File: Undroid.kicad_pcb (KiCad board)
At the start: 4 copper layers, 61.7 x 133.2 mm, 40 parts

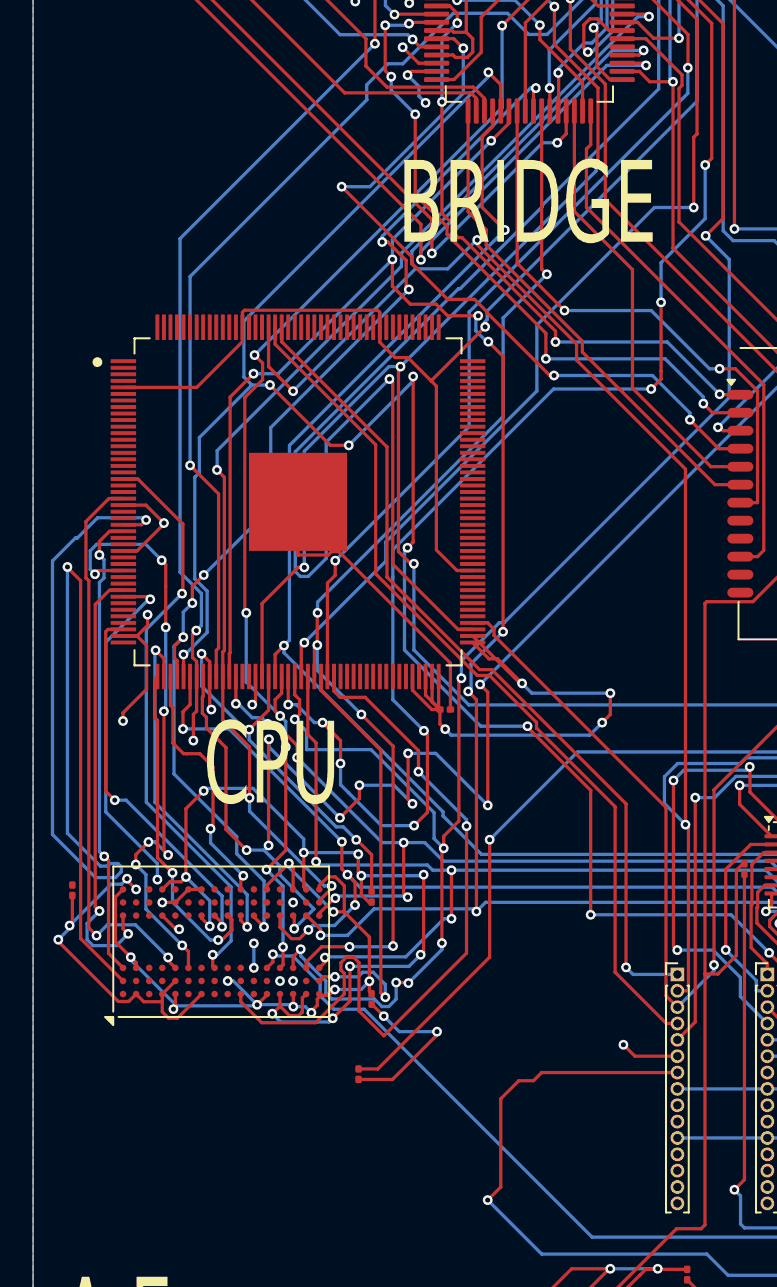
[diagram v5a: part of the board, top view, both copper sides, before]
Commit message: Improving routes.
Signed-off-by: Amlal EL Mahrouss <amlalelmahrouss@icloud.com>
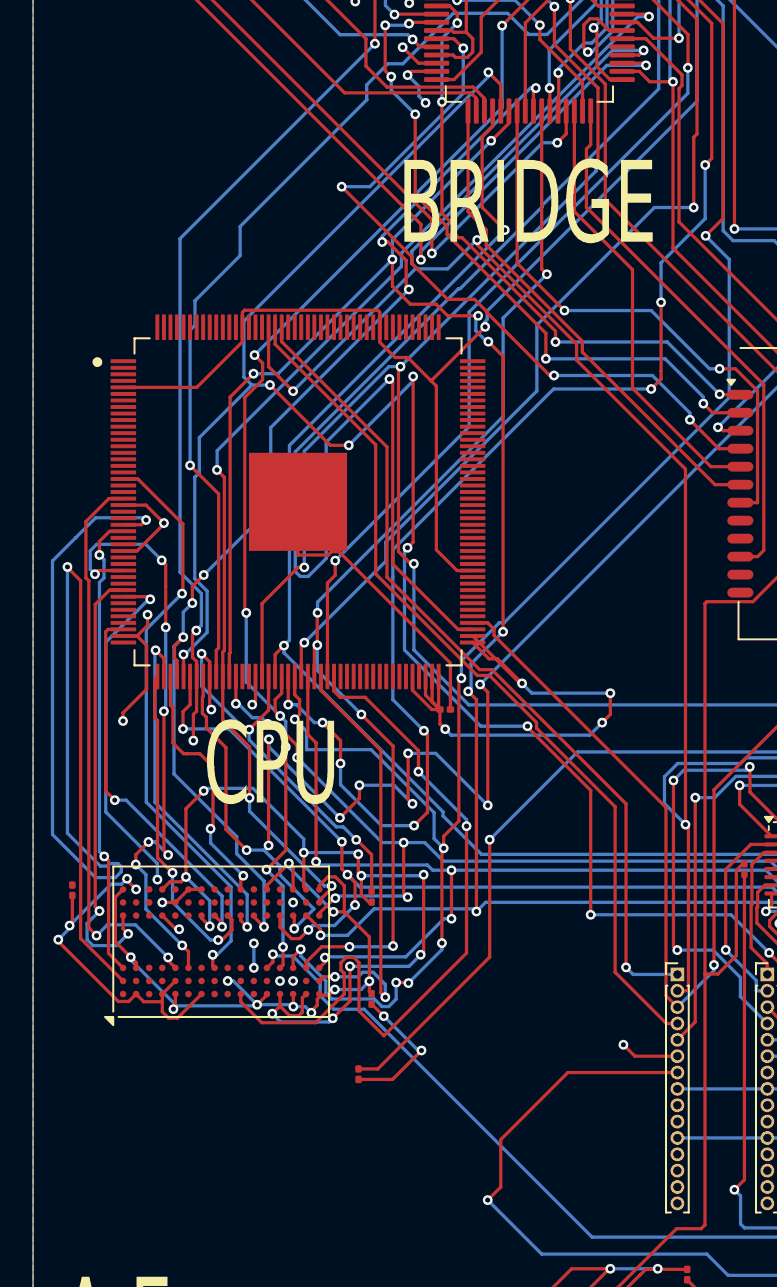
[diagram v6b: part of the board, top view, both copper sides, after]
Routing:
- net GND: track 96.6 -> 94.6 mm
- net GSM_RST_N: track 94.4 -> 92.9 mm
- net GSM_PWR_N: track 57.9 -> 56.6 mm
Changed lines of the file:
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@@
 	)
 	(segment
-		(start 160.3 144.7)
-		(end 157.935001 144.7)
+		(start 146.98 133.12)
+		(end 144.9 133.12)
 		(width 0.2)
 		(layer "F.Cu")
@@
 	)
 	(segment
-		(start 152.88 107.4)
-		(end 153.4 107.4)
+		(start 160.3 144.7)
+		(end 157.935001 144.7)
 		(width 0.2)
 		(layer "F.Cu")
@@
 	)
 	(segment
-		(start 149.7 130.2)
-		(end 149.7 130.4)
+		(start 152.88 107.4)
+		(end 153.4 107.4)
 		(width 0.2)
 		(layer "F.Cu")
@@
 	)
 	(segment
-		(start 149.7 130.4)
-		(end 146.98 133.12)
-		(width 0.2)
-		(layer "F.Cu")
-		(net 4)
-	)
-	(segment
 		(start 149.8 108.48)
 		(end 149.8 110.42)
@@
 	)
 	(segment
-		(start 162.7 66.2)
-		(end 162.475 65.975)
+		(start 148.75 131.35)
+		(end 146.98 133.12)
 		(width 0.2)
 		(layer "F.Cu")
@@
 	)
 	(segment
-		(start 146.98 133.12)
-		(end 144.9 133.12)
+		(start 162.7 66.2)
+		(end 162.475 65.975)
 		(width 0.2)
 		(layer "F.Cu")
@@
 	)
 	(via
-		(at 149.7 130.2)
+		(at 148.75 131.35)
 		(size 0.6)
 		(drill 0.3)
@@
 	)
 	(segment
+		(start 148.75 131.35)
+		(end 148.545818 131.35)
+		(width 0.2)
+		(layer "B.Cu")
+		(net 4)
+	)
+	(segment
 		(start 154.9 108.9)
 		(end 155.5 109.5)
@@
 	)
 	(segment
-		(start 147.395818 130.2)
-		(end 149.7 130.2)
-		(width 0.2)
-		(layer "B.Cu")
-		(net 4)
-	)
-	(segment
 		(start 159.0306 112.0694)
 		(end 150.5694 112.0694)
@@
 	)
 	(segment
-		(start 146.447909 129.252091)
-		(end 147.395818 130.2)
+		(start 148.545818 131.35)
+		(end 146.447909 129.252091)
 		(width 0.2)
 		(layer "B.Cu")
@@
 	)
 	(segment
+		(start 134.90015 87.00015)
+		(end 134.6003 87.3)
+		(width 0.2)
+		(layer "B.Cu")
+		(net 54)
+	)
+	(segment
 		(start 158.6439 65.5486)
 		(end 158.6439 67.0044)
@@
 	)
 	(segment
+		(start 137.66005 80.96005)
+		(end 137.66005 82.74025)
+		(width 0.2)
+		(layer "B.Cu")
+		(net 54)
+	)
+	(segment
 		(start 155.307 69.2172)
 		(end 154.0128 67.923)
@@
 	)
 	(segment
+		(start 137.66005 82.74025)
+		(end 134.90015 85.50015)
+		(width 0.2)
+		(layer "B.Cu")
+		(net 54)
+	)
+	(segment
 		(start 145.4 72.3)
 		(end 145.4 73.2)
@@
 	)
 	(segment
-		(start 134.6003 84.0198)
-		(end 134.6003 95.571)
+		(start 145.41005 73.21005)
+		(end 137.66005 80.96005)
 		(width 0.2)
 		(layer "B.Cu")
@@
 	)
 	(segment
-		(start 145.41005 73.21005)
-		(end 134.6003 84.0198)
+		(start 134.90015 85.50015)
+		(end 134.90015 87.00015)
+		(width 0.2)
+		(layer "B.Cu")
+		(net 54)
+	)
+	(segment
+		(start 134.6003 87.3)
+		(end 134.6003 95.571)
 		(width 0.2)
 		(layer "B.Cu")
@@
 	)
 	(segment
-		(start 127.7143 100.0005)
-		(end 127.7143 100.0006)
+		(start 129.5408 120.0746)
+		(end 129.1113 120.0746)
 		(width 0.2)
 		(layer "B.Cu")
@@
 	)
 	(segment
-		(start 128.8204 120.7783)
-		(end 130.0317 120.7783)
+		(start 130.3946 120.1242)
+		(end 130.1885 119.9181)
 		(width 0.2)
 		(layer "B.Cu")
@@
 	)
 	(segment
-		(start 130.0317 120.7783)
-		(end 130.3946 120.4154)
+		(start 127.1002 101.7833)
+		(end 127.1001 101.7833)
 		(width 0.2)
 		(layer "B.Cu")
@@
 	)
 	(segment
-		(start 129.6973 119.9181)
-		(end 129.5408 120.0746)
+		(start 130.1885 119.9181)
+		(end 129.6973 119.9181)
 		(width 0.2)
 		(layer "B.Cu")
@@
 	)
 	(segment
-		(start 128.9433 98.7715)
-		(end 127.7143 100.0005)
+		(start 129.6973 119.9181)
+		(end 129.5408 120.0746)
 		(width 0.2)
 		(layer "B.Cu")
@@
 	)
 	(segment
-		(start 130.3946 120.1242)
-		(end 130.1885 119.9181)
+		(start 128.8204 120.7783)
+		(end 130.0317 120.7783)
 		(width 0.2)
 		(layer "B.Cu")
@@
 	)
 	(segment
-		(start 131.7724 98.7715)
-		(end 128.9433 98.7715)
+		(start 126.186 118.1439)
+		(end 128.8204 120.7783)
 		(width 0.2)
 		(layer "B.Cu")
@@
 	)
 	(segment
-		(start 130.3946 120.4154)
-		(end 130.3946 120.1242)
+		(start 129.1113 120.0746)
+		(end 127.1002 118.0635)
 		(width 0.2)
 		(layer "B.Cu")
@@
 	)
 	(segment
-		(start 127.1002 118.0635)
-		(end 127.1002 101.7833)
+		(start 127.5994 100.0006)
+		(end 127.5961 100.0006)
 		(width 0.2)
 		(layer "B.Cu")
@@
 	)
 	(segment
-		(start 127.1002 101.7833)
-		(end 127.1001 101.7833)
+		(start 131.7724 98.7715)
+		(end 128.8285 98.7715)
 		(width 0.2)
 		(layer "B.Cu")
@@
 	)
 	(segment
-		(start 129.5408 120.0746)
-		(end 129.1113 120.0746)
+		(start 127.5961 100.0006)
+		(end 126.186 101.4107)
 		(width 0.2)
 		(layer "B.Cu")
@@
 	)
 	(segment
-		(start 129.1113 120.0746)
-		(end 127.1002 118.0635)
-		(width 0.2)
-		(layer "B.Cu")
-		(net 86)
-	)
-	(segment
-		(start 127.7143 100.0006)
-		(end 127.5961 100.0006)
+		(start 127.1002 118.0635)
+		(end 127.1002 101.7833)
 		(width 0.2)
 		(layer "B.Cu")
@@
 	)
 	(segment
-		(start 126.186 101.4107)
-		(end 126.186 118.1439)
+		(start 130.0317 120.7783)
+		(end 130.3946 120.4154)
 		(width 0.2)
 		(layer "B.Cu")
@@
 	)
 	(segment
-		(start 127.5961 100.0006)
-		(end 126.186 101.4107)
+		(start 128.8285 98.7715)
+		(end 127.5994 100.0006)
 		(width 0.2)
 		(layer "B.Cu")
@@
 	)
 	(segment
-		(start 130.1885 119.9181)
-		(end 129.6973 119.9181)
+		(start 130.3946 120.4154)
+		(end 130.3946 120.1242)
 		(width 0.2)
 		(layer "B.Cu")
@@
 	)
 	(segment
-		(start 126.186 118.1439)
-		(end 128.8204 120.7783)
+		(start 126.186 101.4107)
+		(end 126.186 118.1439)
 		(width 0.2)
 		(layer "B.Cu")
@@
 	)
 	(segment
-		(start 170.9 103.6)
-		(end 174.1 103.6)
-		(width 0.2)
-		(layer "In2.Cu")
-		(net 133)
-	)
-	(segment
 		(start 157.9 128.7)
-		(end 157.9 122.8)
+		(end 157.9 118.3)
 		(width 0.2)
 		(layer "In2.Cu")
@@
 	)
 	(segment
-		(start 156.7 121.6)
-		(end 156.7 119.5)
+		(start 166.4 108.6)
+		(end 171.4 103.6)
 		(width 0.2)
 		(layer "In2.Cu")
@@
 	)
 	(segment
-		(start 156.7 119.5)
-		(end 166.4 109.8)
+		(start 161.1 131)
+		(end 160.2 131)
 		(width 0.2)
 		(layer "In2.Cu")
@@
 	)
 	(segment
-		(start 157.9 122.8)
-		(end 156.7 121.6)
+		(start 171.4 103.6)
+		(end 174.1 103.6)
 		(width 0.2)
 		(layer "In2.Cu")
@@
 	)
 	(segment
-		(start 161.1 131)
-		(end 160.2 131)
+		(start 157.9 118.3)
+		(end 166.4 109.8)
 		(width 0.2)
 		(layer "In2.Cu")
@@
 	(segment
 		(start 166.4 109.8)
-		(end 166.4 108.1)
-		(width 0.2)
-		(layer "In2.Cu")
-		(net 133)
-	)
-	(segment
-		(start 166.4 108.1)
-		(end 170.9 103.6)
+		(end 166.4 108.6)
 		(width 0.2)
 		(layer "In2.Cu")
@@
 	)
 	(segment
-		(start 153.6 134.3)
+		(start 153.6 136.8)
 		(end 153.6 139.7)
 		(width 0.2)
@@
 	)
 	(segment
-		(start 164.4 132.7)
-		(end 156.1 132.7)
-		(width 0.2)
-		(layer "F.Cu")
-		(net 181)
-	)
-	(segment
-		(start 155.6 133.2)
-		(end 154.7 133.2)
-		(width 0.2)
-		(layer "F.Cu")
-		(net 181)
-	)
-	(segment
-		(start 156.1 132.7)
-		(end 155.6 133.2)
+		(start 153.6 139.7)
+		(end 152.8 140.5)
 		(width 0.2)
 		(layer "F.Cu")
@@
 	)
 	(segment
-		(start 183.45 96.75)
-		(end 182.3 97.9)
+		(start 157.7 132.7)
+		(end 153.6 136.8)
 		(width 0.2)
 		(layer "F.Cu")
@@
 	)
 	(segment
-		(start 154.7 133.2)
-		(end 153.6 134.3)
+		(start 183.45 96.75)
+		(end 182.3 97.9)
 		(width 0.2)
 		(layer "F.Cu")
@@
 	)
 	(segment
-		(start 153.6 139.7)
-		(end 152.8 140.5)
+		(start 164.4 132.7)
+		(end 157.7 132.7)
 		(width 0.2)
 		(layer "F.Cu")
